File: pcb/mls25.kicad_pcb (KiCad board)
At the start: 4 copper layers, 130 x 40 mm, 179 parts, among them J1 MTJ-88ARX1-FSM-LG, J2 TC2070-FP, J3 SM04B-SRSS-TB, J4 JST B3B-ZR, J5 DC barrel plug, J6 JST B3B-ZR, J7 DC barrel plug, Q1 DMG3406L, Q2 DMG3406L, Q3 DMG3406L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

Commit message: Rename `mls12` to `mls25`
Module output was changed from 12W to 25W during the course of development.
Update filenames to reflect that.
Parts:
- A1: footprint mls12:Ag5724-LPB -> mls25:Ag5724-LPB
- D3, D4: footprint mls12:LMB110S-TP -> mls25:LMB110S-TP
- F1, F2: footprint mls12:SMD1812B050TF_30 -> mls25:SMD1812B050TF_30
- J5, J7: footprint mls12:DC_Barrel_Plug_2.1x5.5mm -> mls25:DC_Barrel_Plug_2.1x5.5mm
- TR1: footprint mls12:7490120110 -> mls25:7490120110
- U1: footprint mls12:DPC817S-C-TR -> mls25:DPC817S-C-TR
- U3: footprint mls12:LMR51606_SOT-23-6 -> mls25:LMR51606_SOT-23-6

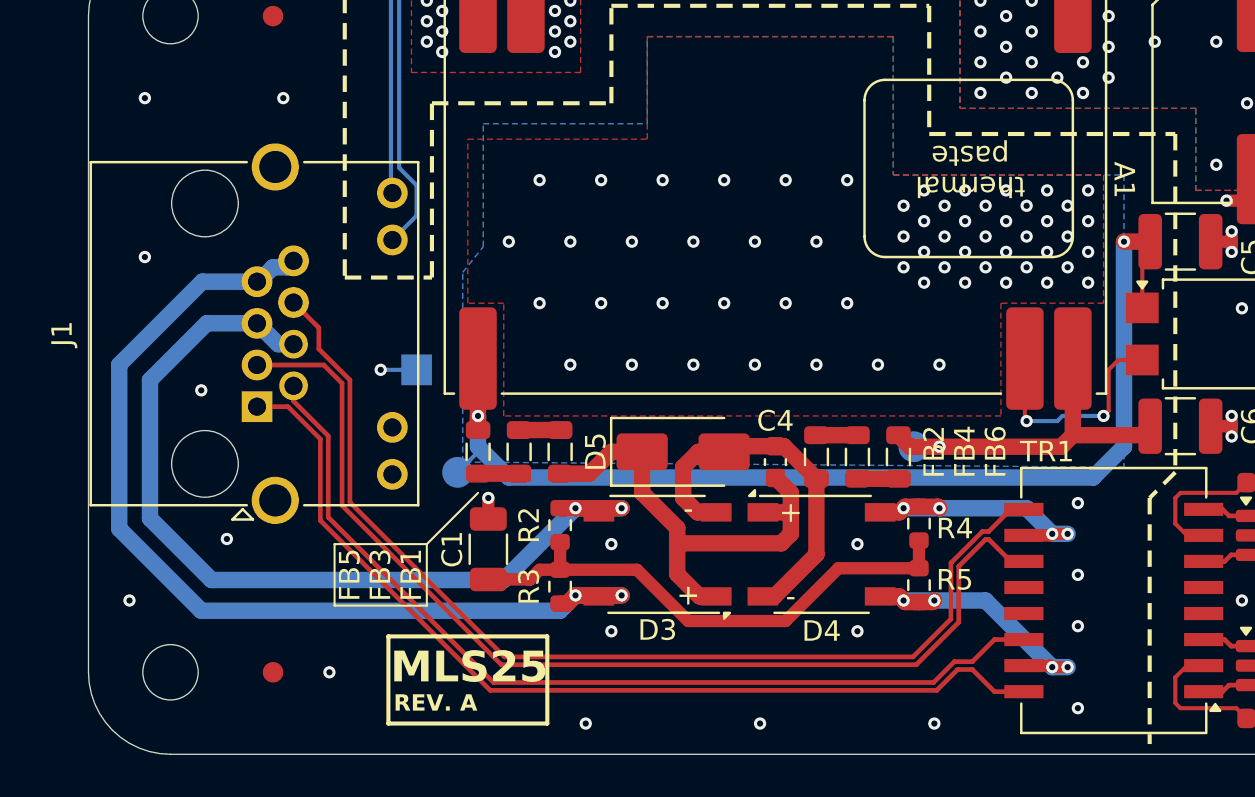
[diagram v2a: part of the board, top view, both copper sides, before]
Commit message: Tweaks/fixes after design review
*  Fix RJ45 refdes on silkscreen.
*  Change PHY IRQ pullup from 1K to 4K7 per datasheet recommendations.
*  Add skew correction on MDI TX differential pair.
*  Remove copper under magnetics.
*  Add annotation that TYP2_DET signal requires MCU internal pullup.
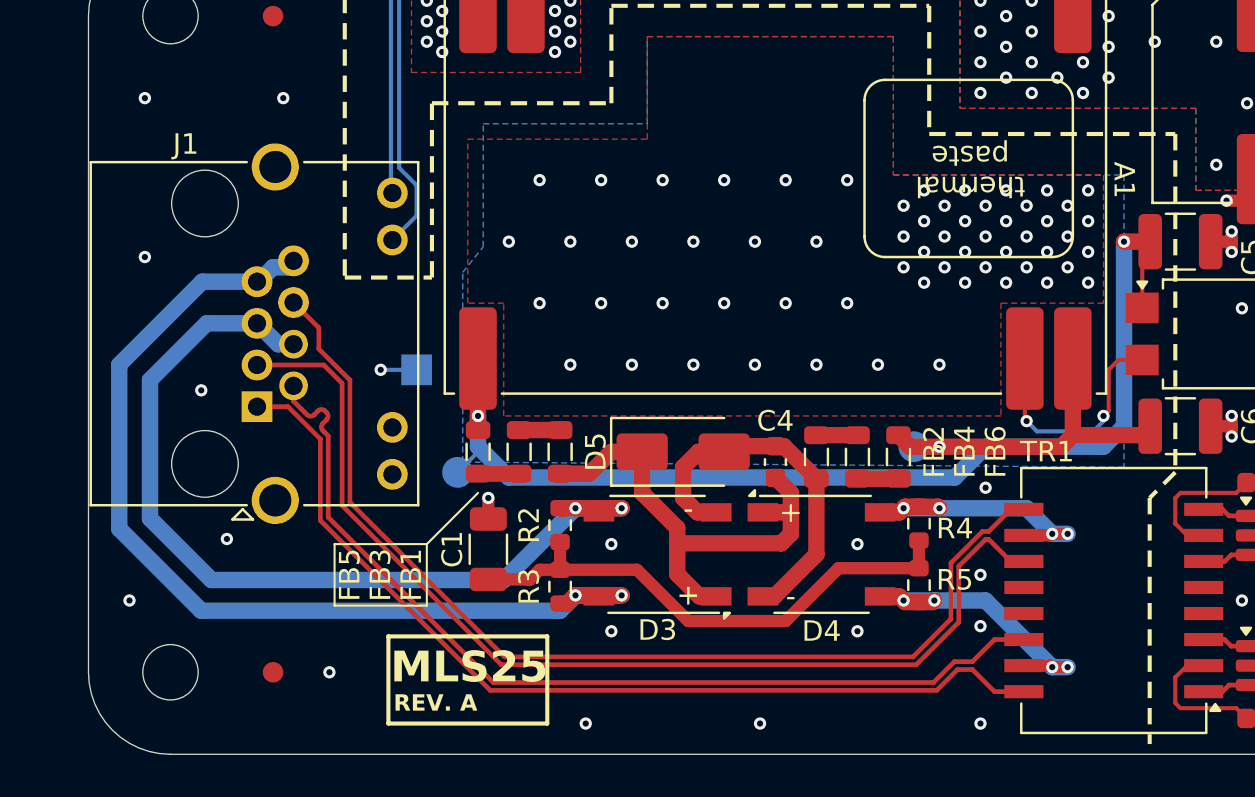
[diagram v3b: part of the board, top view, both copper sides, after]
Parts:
- R13: value 1K -> 4K7
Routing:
- net /ETH-CONN/MDI_TX-: track 45.2 -> 46.3 mm
- net Net-(A1-V_{IN+}): track 54.1 -> 53.5 mm
- net Net-(A1-TYP2-DET): track 11.1 -> 11.7 mm
- net GNDPWR: vias 80 -> 79
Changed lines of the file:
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@@
 		(tags "RJ45 8p8c ethernet cat5")
 		(property "Reference" "J1"
-			(at 3.56 -9.5 90)
+			(at 12.798 -3.47 180)
 			(layer "F.SilkS")
 			(effects
@@
 			)
 		)
-		(property "Value" "1K"
+		(property "Value" "4K7"
 			(at 0 1.43 90)
 			(layer "F.Fab")
@@
 			)
 		)
-		(property "Datasheet" "https://www.mouser.be/datasheet/2/447/PYu_AC_51_RoHS_L_11-3418659.pdf"
+		(property "Datasheet" "https://www.mouser.be/datasheet/2/447/YAGEO_PYu_RC_Group_51_RoHS_L_12-3313492.pdf"
 			(at 0 0 90)
 			(layer "F.Fab")
@@
 			)
 		)
-		(property "MPN" "AC0603JR-131KL"
+		(property "MPN" "RC0603JR-134K7L"
 			(at 0 0 270)
 			(unlocked yes)
@@
 	)
 	(segment
+		(start 153.75 105)
+		(end 152.25 106.5)
+		(width 0.8)
+		(layer "B.Cu")
+		(net 2)
+	)
+	(segment
 		(start 128.995 103.5)
 		(end 128.995 104.995)
@@
 	)
 	(segment
-		(start 128.995 104.995)
-		(end 130.5 106.5)
+		(start 160.5 104)
+		(end 160.5 95)
 		(width 0.8)
 		(layer "B.Cu")
@@
 	)
 	(segment
-		(start 160.5 105)
-		(end 160.5 95)
+		(start 159.5 105)
+		(end 153.75 105)
 		(width 0.8)
 		(layer "B.Cu")
@@
 	)
 	(segment
-		(start 159 106.5)
-		(end 160.5 105)
+		(start 128.995 104.995)
+		(end 130.5 106.5)
 		(width 0.8)
 		(layer "B.Cu")
@@
 	(segment
 		(start 130.5 106.5)
-		(end 159 106.5)
+		(end 152.25 106.5)
+		(width 0.8)
+		(layer "B.Cu")
+		(net 2)
+	)
+	(segment
+		(start 159.5 105)
+		(end 160.5 104)
 		(width 0.8)
 		(layer "B.Cu")
@@
 	)
 	(segment
-		(start 157.25 103.75)
-		(end 155.75 103.75)
+		(start 159.5 103.5)
+		(end 159.5 103.75)
 		(width 0.2)
 		(layer "B.Cu")
@@
 	)
 	(segment
-		(start 159.5 103.5)
-		(end 157.5 103.5)
+		(start 159 104.25)
+		(end 156.25 104.25)
 		(width 0.2)
 		(layer "B.Cu")
@@
 	)
 	(segment
-		(start 157.5 103.5)
-		(end 157.25 103.75)
+		(start 159.5 103.75)
+		(end 159 104.25)
+		(width 0.2)
+		(layer "B.Cu")
+		(net 6)
+	)
+	(segment
+		(start 156.25 104.25)
+		(end 155.75 103.75)
 		(width 0.2)
 		(layer "B.Cu")
@@
 	)
 	(via
-		(at 151.25 118.5)
+		(at 153.5 118.5)
 		(size 0.6)
 		(drill 0.3)
@@
 	)
 	(via
-		(at 158.25 113.75)
+		(at 153.5 113.75)
 		(size 0.6)
 		(drill 0.3)
@@
 	)
 	(via
-		(at 158.25 107.75)
+		(at 153.75 107)
 		(size 0.6)
 		(drill 0.3)
@@
 	)
 	(via
-		(at 158.25 111.25)
+		(at 153.5 111.25)
 		(size 0.6)
 		(drill 0.3)
@@
 	)
 	(via
-		(at 158.25 117.75)
-		(size 0.6)
-		(drill 0.3)
-		(layers "F.Cu" "B.Cu")
-		(free yes)
-		(net 7)
-	)
-	(via
 		(at 156.75 94)
 		(size 0.6)
@@
 	)
 	(segment
-		(start 121.690701 104.469009)
-		(end 120 102.778308)
+		(start 121.428197 104.206506)
+		(end 121.513051 104.291359)
+		(width 0.228464)
+		(layer "F.Cu")
+		(net 135)
+	)
+	(segment
+		(start 121.532037 103.25414)
+		(end 121.616889 103.338992)
 		(width 0.228464)
 		(layer "F.Cu")
@@
 	(segment
 		(start 121.690701 108.439289)
-		(end 121.690701 104.469009)
+		(end 129.750413 116.499001)
 		(width 0.228464)
 		(layer "F.Cu")
@@
 	)
 	(segment
-		(start 154.182499 114.405)
-		(end 153.1042 115.483299)
+		(start 121.690701 104.469009)
+		(end 121.690701 108.439289)
 		(width 0.228464)
 		(layer "F.Cu")
@@
 	)
 	(segment
-		(start 152.225905 115.483299)
+		(start 121.616889 103.678404)
+		(end 121.428196 103.867094)
+		(width 0.228464)
+		(layer "F.Cu")
+		(net 135)
+	)
+	(segment
+		(start 121.003935 103.442832)
+		(end 121.192625 103.254139)
+		(width 0.228464)
+		(layer "F.Cu")
+		(net 135)
+	)
+	(segment
+		(start 129.750413 116.499001)
 		(end 151.210203 116.499001)
 		(width 0.228464)
@@
 	)
 	(segment
-		(start 151.210203 116.499001)
-		(end 129.750413 116.499001)
+		(start 153.1042 115.483299)
+		(end 154.182499 114.405)
 		(width 0.228464)
 		(layer "F.Cu")
@@
 	)
 	(segment
-		(start 155.615 114.405)
-		(end 154.182499 114.405)
+		(start 120.533335 103.311643)
+		(end 120.664523 103.442831)
 		(width 0.228464)
 		(layer "F.Cu")
@@
 	)
 	(segment
-		(start 129.750413 116.499001)
-		(end 121.690701 108.439289)
+		(start 151.210203 116.499001)
+		(end 152.225905 115.483299)
 		(width 0.228464)
 		(layer "F.Cu")
@@
 	)
 	(segment
-		(start 153.1042 115.483299)
-		(end 152.225905 115.483299)
+		(start 120.533335 103.311643)
+		(end 120.39729 103.175598)
+		(width 0.228464)
+		(layer "F.Cu")
+		(net 135)
+	)
+	(segment
+		(start 152.225905 115.483299)
+		(end 153.1042 115.483299)
+		(width 0.228464)
+		(layer "F.Cu")
+		(net 135)
+	)
+	(segment
+		(start 154.182499 114.405)
+		(end 155.615 114.405)
+		(width 0.228464)
+		(layer "F.Cu")
+		(net 135)
+	)
+	(segment
+		(start 121.513051 104.291359)
+		(end 121.690701 104.469009)
+		(width 0.228464)
+		(layer "F.Cu")
+		(net 135)
+	)
+	(segment
+		(start 120.39729 103.175598)
+		(end 120 102.778308)
+		(width 0.228464)
+		(layer "F.Cu")
+		(net 135)
+	)
+	(arc
+		(start 121.616889 103.338992)
+		(mid 121.687183 103.508697)
+		(end 121.616889 103.678404)
+		(width 0.228464)
+		(layer "F.Cu")
+		(net 135)
+	)
+	(arc
+		(start 121.192625 103.254139)
+		(mid 121.362331 103.183846)
+		(end 121.532037 103.25414)
+		(width 0.228464)
+		(layer "F.Cu")
+		(net 135)
+	)
+	(arc
+		(start 120.664523 103.442831)
+		(mid 120.834229 103.513125)
+		(end 121.003935 103.442832)
+		(width 0.228464)
+		(layer "F.Cu")
+		(net 135)
+	)
+	(arc
+		(start 121.428196 103.867094)
+		(mid 121.357903 104.0368)
+		(end 121.428197 104.206506)
 		(width 0.228464)
 		(layer "F.Cu")
@@
 			(pts
 				(xy 105 75) (xy 121 75) (xy 121 97.25) (xy 122.5 98.75) (xy 128.5 98.75) (xy 128.5 90) (xy 149.25 90)
-				(xy 149.25 91.75) (xy 160.25 91.75) (xy 160.25 125) (xy 105 125)
+				(xy 149.25 91.75) (xy 160.25 91.75) (xy 160.25 106) (xy 155.5 106) (xy 155.5 125) (xy 105 125)
 			)
 		)
@@
 		(base_line
 			(pts
+				(xy 120.533335 103.311643) (xy 120.39729 103.175598)
+			)
+		)
+		(base_line_coupled
+			(pts
+				(xy 120.263643 103.581335) (xy 120.268502 103.586194)
+			)
+		)
+		(corner_radius_percent 80)
+		(end
+			(xy 120.39729 103.175598)
+		)
+		(initial_side "right")
+		(last_diff_pair_gap 0.18)
+		(last_netname "/ETH-CONN/MDI_TX-")
+		(last_status "too_short")
+		(last_track_width 0.228464)
+		(last_tuning "-1.0816 mm (too short)")
+		(max_amplitude 1)
+		(min_amplitude 0.2)
+		(min_spacing 0.6)
+		(origin
+			(xy 120.533335 103.311643)
+		)
+		(override_custom_rules no)
+		(rounded yes)
+		(single_sided no)
+		(target_length 1000000)
+		(target_length_max 1000000)
+		(target_length_min 0)
+		(target_skew 0)
+		(target_skew_max 0.1)
+		(target_skew_min -0.1)
+		(tuning_mode "diff_pair_skew")
+		(members "aff6e21a-93d7-4bfa-bf6d-c4d549983e6b")
+	)
+	(generated
+		(type tuning_pattern)
+		(name "Tuning Pattern")
+		(layer "F.Cu")
+		(base_line
+			(pts
 				(xy 187.572718 114.25) (xy 191 114.25)
 			)
@@
 		)
 	)
+	(generated
+		(type tuning_pattern)
+		(name "Tuning Pattern")
+		(layer "F.Cu")
+		(base_line
+			(pts
+				(xy 120.664523 103.442831) (xy 121.690701 104.469009)
+			)
+		)
+		(base_line_coupled
+			(pts
+				(xy 120.394831 103.712523) (xy 120.39969 103.717382)
+			)
+		)
+		(corner_radius_percent 80)
+		(end
+			(xy 121.690701 104.469009)
+		)
+		(initial_side "left")
+		(last_diff_pair_gap 0.18)
+		(last_netname "/ETH-CONN/MDI_TX-")
+		(last_status "too_short")
+		(last_track_width 0.228464)
+		(last_tuning "-0.0000 mm (too short)")
+		(max_amplitude 1)
+		(min_amplitude 0.2)
+		(min_spacing 0.6)
+		(origin
+			(xy 120.664523 103.442831)
+		)
+		(override_custom_rules no)
+		(rounded yes)
+		(single_sided no)
+		(target_length 1000000)
+		(target_length_max 1000000)
+		(target_length_min 0)
+		(target_skew 0)
+		(target_skew_max 2147.483647)
+		(target_skew_min 0)
+		(tuning_mode "diff_pair_skew")
+		(members "173ee95f-5a0b-4ac7-9a59-80419255ec23" "1f10c7ae-7bf3-460b-9771-2bf056c7df77"
+			"20705ed9-0ce2-464c-b860-0c1483122624" "5584080a-526e-45f0-aacc-f1a6e9b390fd"
+			"6cec9b74-bf28-47ee-947a-60f93b87641e" "795a9ac9-c1d2-47de-ae92-6298d6e0106f"
+			"7f4567d2-e498-443f-9059-c2a79210ecf0" "a9e07005-ad96-4bad-8123-b779e5891c48"
+			"d808bbe6-b2aa-46b8-9241-1dc4ff52283d"
+		)
+	)

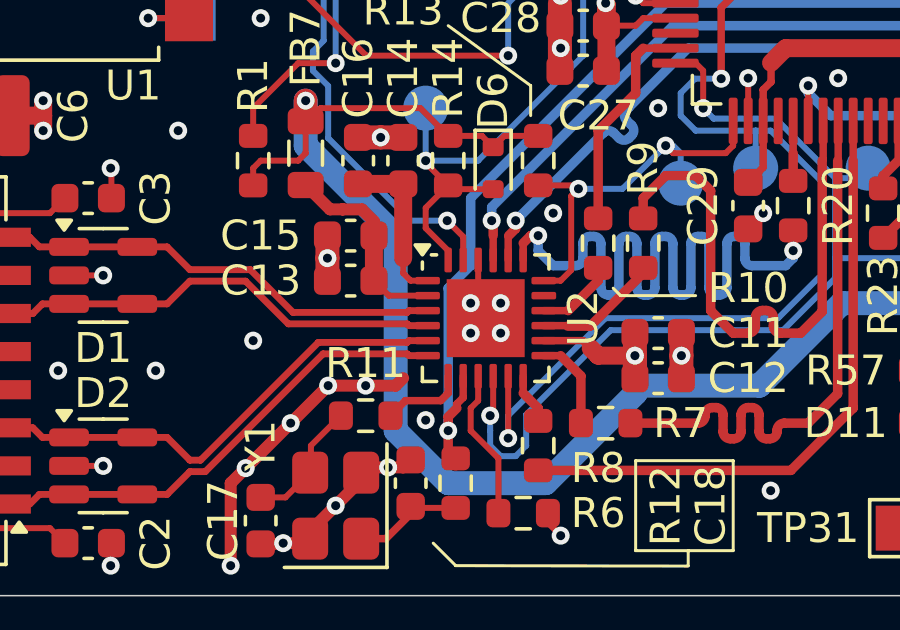
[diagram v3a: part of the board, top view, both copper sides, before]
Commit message: Change PHY to datasheet recommended footprint
Default footprint in the Kicad libraries for KSZ8081 deviates from the
datasheet recommendations. QFN parts can be fiddly, so it's best to stick
closely to the recommendations:

*  Pads are much shorter and a bit thinner.
*  Solder stencil openings for exposed pad are smaller, spaced out a bit less.
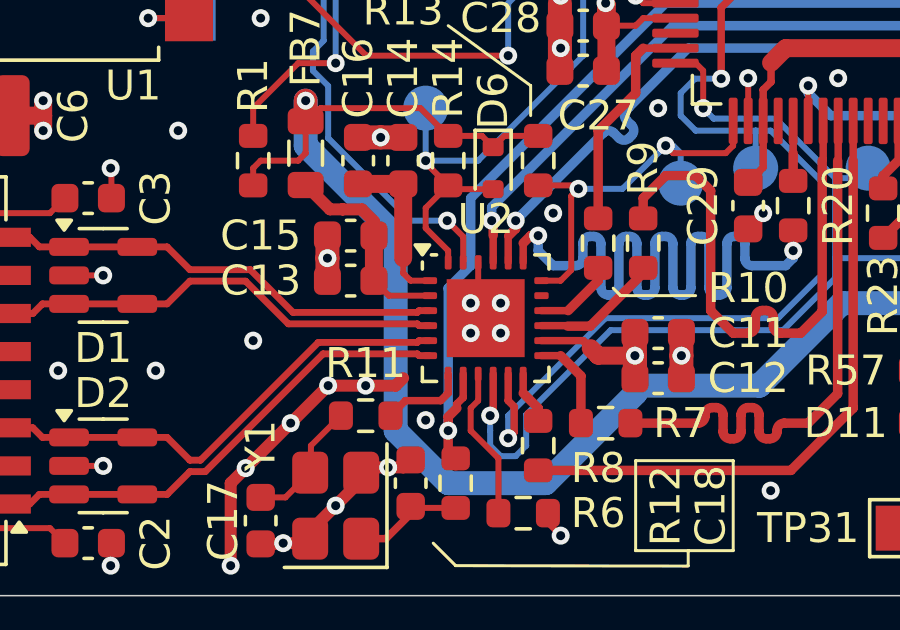
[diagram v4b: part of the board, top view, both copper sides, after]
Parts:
- U2: footprint Package_DFN_QFN:QFN-24-1EP_4x4mm_P0.5mm_EP2.6x2.6mm -> mls25:KSZ8081_QFN-24-1EP_4x4mm_P0.5mm_EP2.6x2.6mm

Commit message: Change output polyfuse from 500mA to 750mA
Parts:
- F1, F2: value 500mA/30V -> 750mA/24V
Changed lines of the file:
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@@
 			)
 		)
-		(property "TODO" ""
-			(at 0 0 0)
-			(unlocked yes)
-			(layer "F.Fab")
-			(hide yes)
-			(effects
-				(font
-					(size 1 1)
-					(thickness 0.15)
-				)
-			)
-		)
 		(property ki_fp_filters "SOT?23*")
 		(sheetname "/ETH-CONN/")
@@
 			)
 		)
-		(property "TODO" ""
-			(at 0 0 0)
-			(unlocked yes)
-			(layer "F.Fab")
-			(hide yes)
-			(effects
-				(font
-					(size 1 1)
-					(thickness 0.15)
-				)
-			)
-		)
 		(property ki_fp_filters "SOT?23*")
 		(sheetname "/ETH-CONN/")
@@
 			)
 		)
-		(property "Value" "500mA/30V"
+		(property "Value" "750mA/24V"
 			(at 0 2.65 0)
 			(layer "F.Fab")
@@
 			)
 		)
-		(property "MPN" "SMD1812B050TF/30"
+		(property "MPN" "SMD1812B075TF/24"
 			(at 0 0 0)
 			(unlocked yes)
@@
 			)
 		)
-		(property "TODO" ""
-			(at 0 0 90)
-			(unlocked yes)
-			(layer "F.Fab")
-			(hide yes)
-			(effects
-				(font
-					(size 1 1)
-					(thickness 0.15)
-				)
-			)
-		)
 		(property ki_fp_filters "Connector*:*_1x??_*")
 		(sheetname "/MCU/")
@@
 			)
 		)
-		(property "Value" "500mA/30V"
+		(property "Value" "750mA/24V"
 			(at 0 2.65 0)
 			(layer "F.Fab")
@@
 			)
 		)
-		(property "MPN" "SMD1812B050TF/30"
+		(property "MPN" "SMD1812B075TF/24"
 			(at 0 0 0)
 			(unlocked yes)
@@
 			)
 		)
-		(property "Datasheet" ""
+		(property "Datasheet" "http://ww1.microchip.com/downloads/en/DeviceDoc/00002199A.pdf"
 			(at 0 0 0)
 			(layer "F.Fab")
@@
 			)
 		)
-		(property "Description" ""
+		(property "Description" "10BASE-T/100BASE-TX PHY with RMII Support, 25 MHz input clock/50 MHz output, QFN-24"
 			(at 0 0 0)
 			(layer "F.Fab")
